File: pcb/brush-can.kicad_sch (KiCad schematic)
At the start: 30 parts, among them J1 Conn_ARM_SWD_TagConnect_TC203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, J2 Conn_01x04_MountingPin, J3 Conn_01x04_MountingPin, U1 AP62150Z6, U2 NCP176, U3 STM32G431CBUx, U4 TJA1044GTK/3, Y1 16MHz

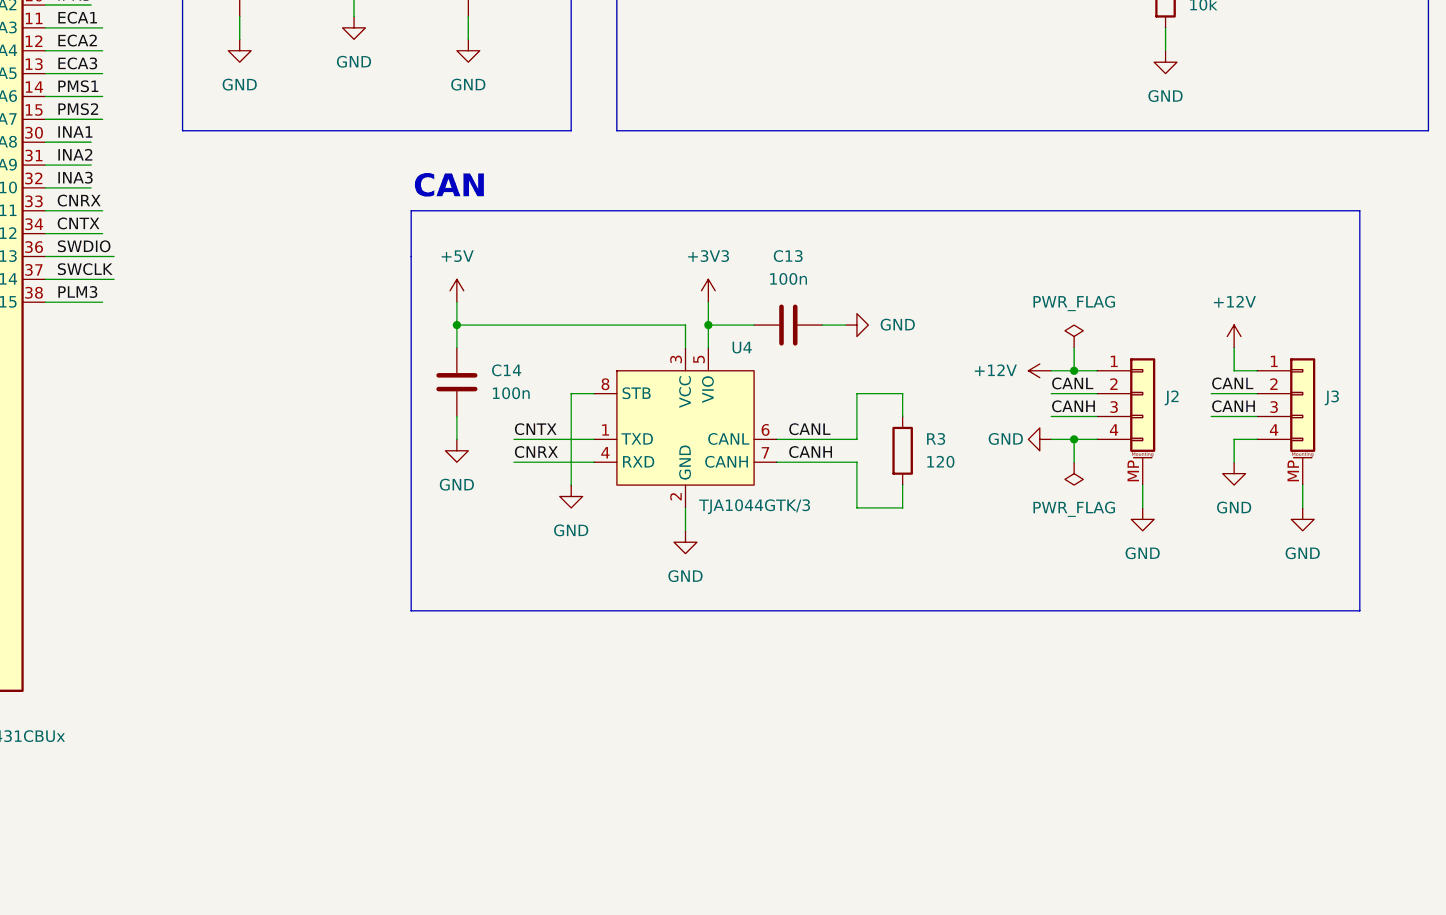
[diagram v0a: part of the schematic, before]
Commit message: Add inserts and change CAN connection
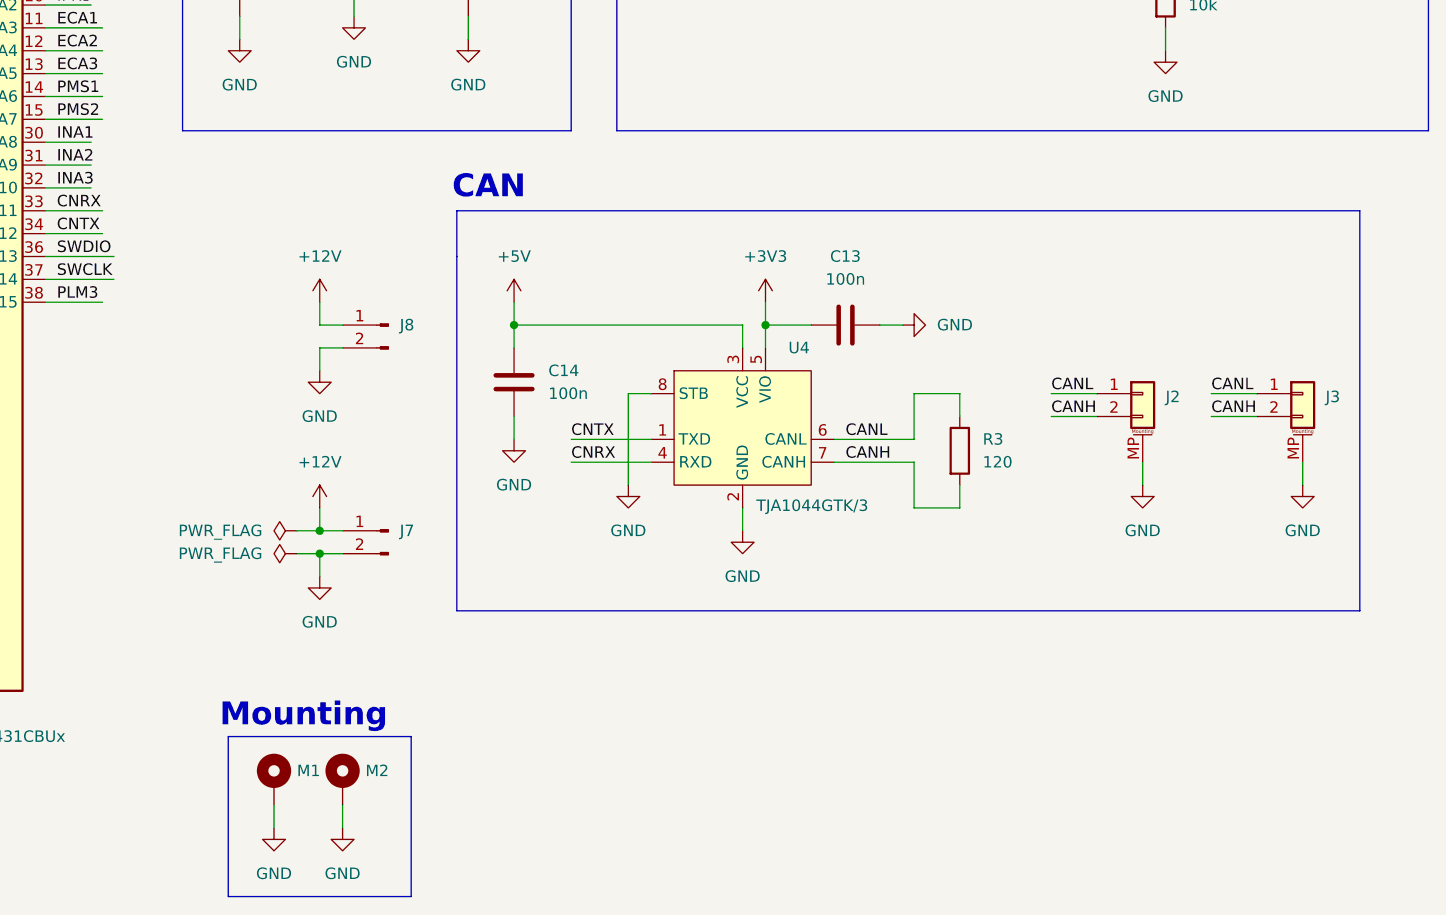
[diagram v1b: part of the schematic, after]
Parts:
- removed J2, J3: Conn_01x04_MountingPin, Connector_JST:JST_GH_SM04B-GHS-TB_1x04-1MP_P1.25mm_Horizontal, symbol Connector_Generic_MountingPin:Conn_01x04_MountingPin
- added J2, J3: Conn_01x02_MountingPin, Connector_JST:JST_SH_SM02B-SRSS-TB_1x02-1MP_P1.00mm_Horizontal, symbol Connector_Generic_MountingPin:Conn_01x02_MountingPin
- added J7, J8: Conn_01x02_Pin, Connector_PinHeader_2.54mm:PinHeader_1x02_P2.54mm_Vertical, symbol Connector:Conn_01x02_Pin
- added M1, M2: 24939, User_Footprints:24939, symbol User_Symbols:24939
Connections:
- net +12V: now also J7.1 (Pin_1), J8.1 (Pin_1)
- net CANH: now also J2.2 (Pin_2), J3.2 (Pin_2)
- net CANL: now also J2.1 (Pin_1), J3.1 (Pin_1)
- net GND: now also J2.MP (MountPin), J3.MP (MountPin), J7.2 (Pin_2), J8.2 (Pin_2), M1.MP, M2.MP
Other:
- note added: "Mounting"
- moved on the sheet: C13, C14, R3, U4

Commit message: Finish layout
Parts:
- removed C2: 100n, Capacitor_SMD:C_0402_1005Metric, symbol Device:C
- C1: footprint Capacitor_SMD:C_0603_1608Metric -> Capacitor_SMD:C_0402_1005Metric
- J7, J8: footprint Connector_PinHeader_2.54mm:PinHeader_1x02_P2.54mm_Vertical -> User_Footprints:PowerPins
- L1: footprint Inductor_SMD:L_Sunlord_MWSA0412S -> Inductor_SMD:L_Chilisin_BMRA00040420; LCSC (none) -> C207829
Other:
- moved on the sheet: C1
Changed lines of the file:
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@@
 	)
 	(junction
-		(at 33.02 78.74)
-		(diameter 0)
-		(color 0 0 0 0)
-	)
-	(junction
 		(at 109.22 81.28)
 		(diameter 0)
@@
 	)
 	(junction
-		(at 45.72 66.04)
-		(diameter 0)
-		(color 0 0 0 0)
-	)
-	(junction
 		(at 264.16 71.12)
 		(diameter 0)
@@
 	(wire
 		(pts
-			(xy 33.02 66.04) (xy 45.72 66.04)
-		)
-		(stroke
-			(width 0)
-			(type default)
-		)
-	)
-	(wire
-		(pts
 			(xy 82.55 35.56) (xy 88.9 35.56)
 		)
@@
 	(wire
 		(pts
+			(xy 45.72 78.74) (xy 45.72 81.28)
+		)
+		(stroke
+			(width 0)
+			(type default)
+		)
+	)
+	(wire
+		(pts
 			(xy 90.17 129.54) (xy 96.52 129.54)
 		)
@@
 	(wire
 		(pts
-			(xy 33.02 78.74) (xy 45.72 78.74)
-		)
-		(stroke
-			(width 0)
-			(type default)
-		)
-	)
-	(wire
-		(pts
 			(xy 129.54 121.92) (xy 137.16 121.92)
 		)
@@
 	(wire
 		(pts
-			(xy 33.02 78.74) (xy 33.02 81.28)
-		)
-		(stroke
-			(width 0)
-			(type default)
-		)
-	)
-	(wire
-		(pts
 			(xy 44.45 166.37) (xy 41.91 166.37)
 		)
@@
 	(wire
 		(pts
-			(xy 33.02 68.58) (xy 33.02 66.04)
-		)
-		(stroke
-			(width 0)
-			(type default)
-		)
-	)
-	(wire
-		(pts
 			(xy 129.54 114.3) (xy 134.62 114.3)
 		)
@@
 	(wire
 		(pts
-			(xy 33.02 78.74) (xy 33.02 76.2)
-		)
-		(stroke
-			(width 0)
-			(type default)
-		)
-	)
-	(wire
-		(pts
 			(xy 133.35 27.94) (xy 139.7 27.94)
 		)
@@
 	)
 	(symbol
-		(lib_id "Device:C")
-		(at 45.72 72.39 0)
-		(unit 1)
-		(exclude_from_sim no)
-		(in_bom yes)
-		(on_board yes)
-		(dnp no)
-		(fields_autoplaced yes)
-		(property "Reference" "C2"
-			(at 49.53 71.12 0)
-			(effects
-				(font
-					(size 1.27 1.27)
-				)
-				(justify left)
-			)
-		)
-		(property "Value" "100n"
-			(at 49.53 73.66 0)
-			(effects
-				(font
-					(size 1.27 1.27)
-				)
-				(justify left)
-			)
-		)
-		(property "Footprint" "Capacitor_SMD:C_0402_1005Metric"
-			(at 46.6852 76.2 0)
-			(effects
-				(font
-					(size 1.27 1.27)
-				)
-				(hide yes)
-			)
-		)
-		(property "Datasheet" "~"
-			(at 45.72 72.39 0)
-			(effects
-				(font
-					(size 1.27 1.27)
-				)
-				(hide yes)
-			)
-		)
-		(property "Description" ""
-			(at 45.72 72.39 0)
-			(effects
-				(font
-					(size 1.27 1.27)
-				)
-				(hide yes)
-			)
-		)
-		(pin "1"
-		)
-		(pin "2"
-		)
-		(instances
-			(project "brush-can"
-				(path "/91e4682e-33ab-4e83-b6e9-9501af34d25d"
-					(reference "C2")
-					(unit 1)
-				)
-			)
-		)
-	)
-	(symbol
 		(lib_id "power:GND")
 		(at 181.61 142.24 0)
@@
 			)
 		)
-		(property "Footprint" "Inductor_SMD:L_Sunlord_MWSA0412S"
+		(property "Footprint" "Inductor_SMD:L_Chilisin_BMRA00040420"
 			(at 247.65 71.12 0)
 			(effects
@@
 			)
 		)
+		(property "LCSC" "C207829"
+			(at 247.65 71.12 90)
+			(effects
+				(font
+					(size 1.27 1.27)
+				)
+				(hide yes)
+			)
+		)
 		(pin "1"
 		)
@@
 	(symbol
 		(lib_id "Device:C")
-		(at 33.02 72.39 0)
+		(at 45.72 72.39 0)
 		(unit 1)
 		(exclude_from_sim no)
@@
 		(fields_autoplaced yes)
 		(property "Reference" "C1"
-			(at 36.83 71.12 0)
+			(at 49.53 71.12 0)
 			(effects
 				(font
@@
 		)
 		(property "Value" "10u"
-			(at 36.83 73.66 0)
+			(at 49.53 73.66 0)
 			(effects
 				(font
@@
 			)
 		)
-		(property "Footprint" "Capacitor_SMD:C_0603_1608Metric"
-			(at 33.9852 76.2 0)
+		(property "Footprint" "Capacitor_SMD:C_0402_1005Metric"
+			(at 46.6852 76.2 0)
 			(effects
 				(font
@@
 		)
 		(property "Datasheet" "~"
-			(at 33.02 72.39 0)
+			(at 45.72 72.39 0)
 			(effects
 				(font
@@
 		)
 		(property "Description" ""
-			(at 33.02 72.39 0)
+			(at 45.72 72.39 0)
 			(effects
 				(font
@@
 	)
 	(symbol
+		(lib_id "power:GND")
+		(at 45.72 81.28 0)
+		(unit 1)
+		(exclude_from_sim no)
+		(in_bom yes)
+		(on_board yes)
+		(dnp no)
+		(fields_autoplaced yes)
+		(property "Reference" "#PWR04"
+			(at 45.72 87.63 0)
+			(effects
+				(font
+					(size 1.27 1.27)
+				)
+				(hide yes)
+			)
+		)
+		(property "Value" "GND"
+			(at 45.72 86.36 0)
+			(effects
+				(font
+					(size 1.27 1.27)
+				)
+			)
+		)
+		(property "Footprint" ""
+			(at 45.72 81.28 0)
+			(effects
+				(font
+					(size 1.27 1.27)
+				)
+				(hide yes)
+			)
+		)
+		(property "Datasheet" ""
+			(at 45.72 81.28 0)
+			(effects
+				(font
+					(size 1.27 1.27)
+				)
+				(hide yes)
+			)
+		)
+		(property "Description" ""
+			(at 45.72 81.28 0)
+			(effects
+				(font
+					(size 1.27 1.27)
+				)
+				(hide yes)
+			)
+		)
+		(pin "1"
+		)
+		(instances
+			(project "brush-can"
+				(path "/91e4682e-33ab-4e83-b6e9-9501af34d25d"
+					(reference "#PWR04")
+					(unit 1)
+				)
+			)
+		)
+	)
+	(symbol
 		(lib_id "Device:C")
 		(at 176.53 91.44 0)
@@
 			)
 		)
-		(property "Footprint" "Connector_PinHeader_2.54mm:PinHeader_1x02_P2.54mm_Vertical"
+		(property "Footprint" "User_Footprints:PowerPins"
 			(at 167.64 129.54 0)
 			(effects
@@
 			)
 		)
-		(property "Footprint" "Connector_PinHeader_2.54mm:PinHeader_1x02_P2.54mm_Vertical"
+		(property "Footprint" "User_Footprints:PowerPins"
 			(at 167.64 152.4 0)
 			(effects
@@
 					(unit 1)
 				)
-			)
-		)
-	)
-	(symbol
-		(lib_id "power:GND")
-		(at 33.02 81.28 0)
-		(unit 1)
-		(exclude_from_sim no)
-		(in_bom yes)
-		(on_board yes)
-		(dnp no)
-		(fields_autoplaced yes)
-		(property "Reference" "#PWR04"
-			(at 33.02 87.63 0)
-			(effects
-				(font
-					(size 1.27 1.27)
-				)
-				(hide yes)
-			)
-		)
-		(property "Value" "GND"
-			(at 33.02 86.36 0)
-			(effects
-				(font
-					(size 1.27 1.27)
-				)
-			)
-		)
-		(property "Footprint" ""
-			(at 33.02 81.28 0)
-			(effects
-				(font
-					(size 1.27 1.27)
-				)
-				(hide yes)
-			)
-		)
-		(property "Datasheet" ""
-			(at 33.02 81.28 0)
-			(effects
-				(font
-					(size 1.27 1.27)
-				)
-				(hide yes)
-			)
-		)
-		(property "Description" ""
-			(at 33.02 81.28 0)
-			(effects
-				(font
-					(size 1.27 1.27)
-				)
-				(hide yes)
-			)
-		)
-		(pin "1"
-		)
-		(instances
-			(project "brush-can"
-				(path "/91e4682e-33ab-4e83-b6e9-9501af34d25d"
-					(reference "#PWR04")
-					(unit 1)
-				)

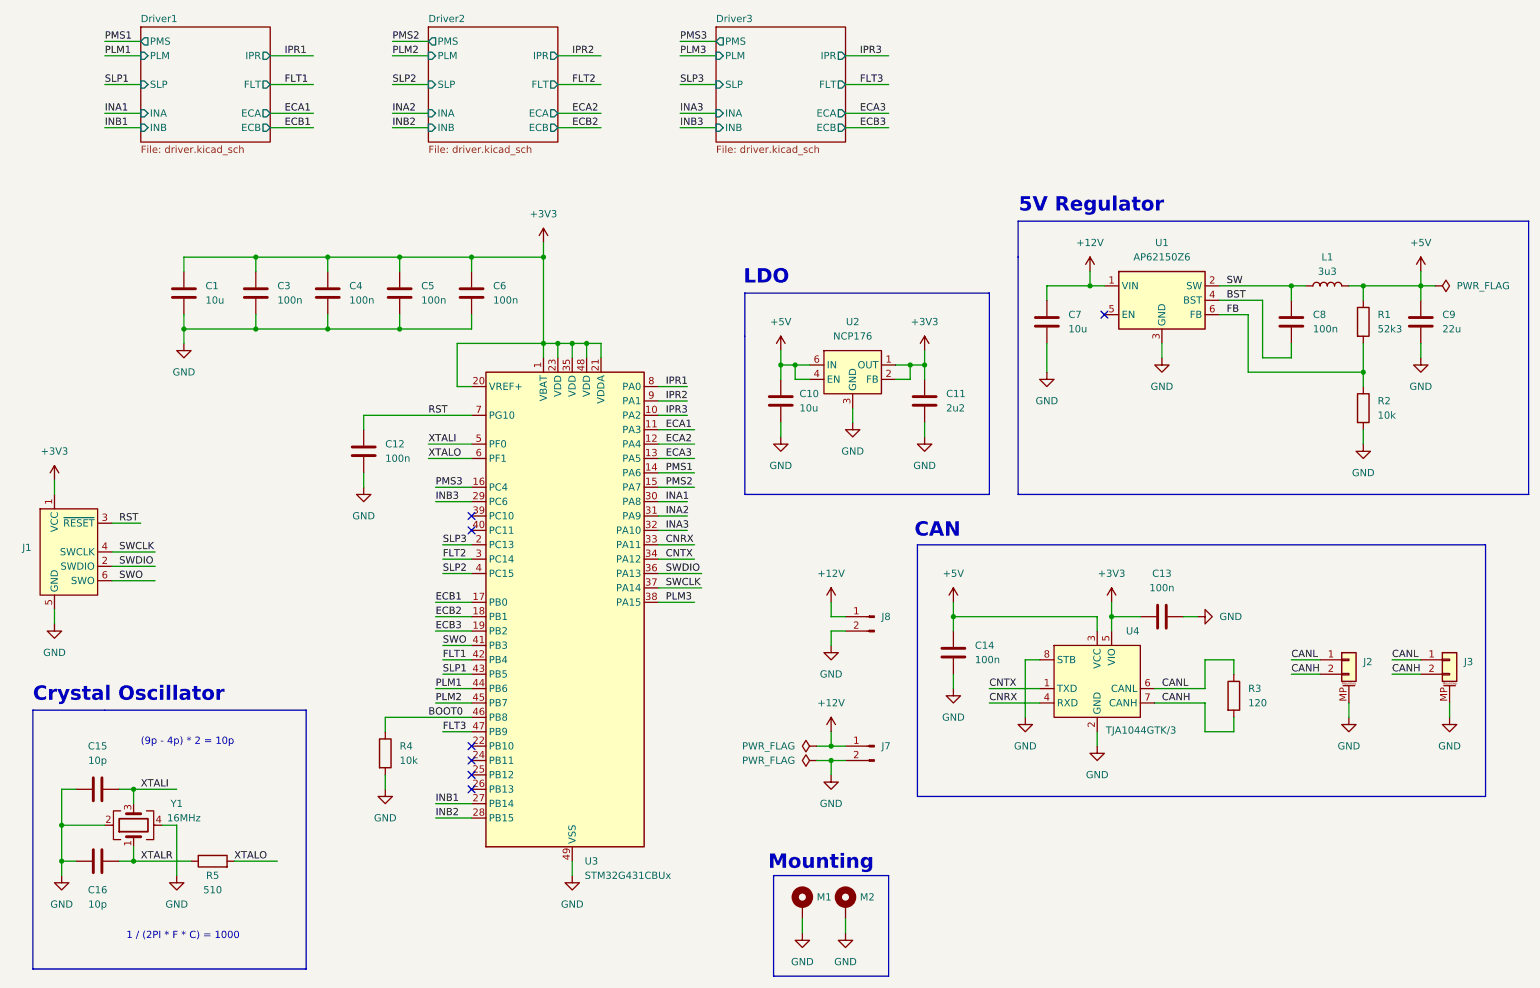
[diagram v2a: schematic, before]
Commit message: Finish routing and rule checking
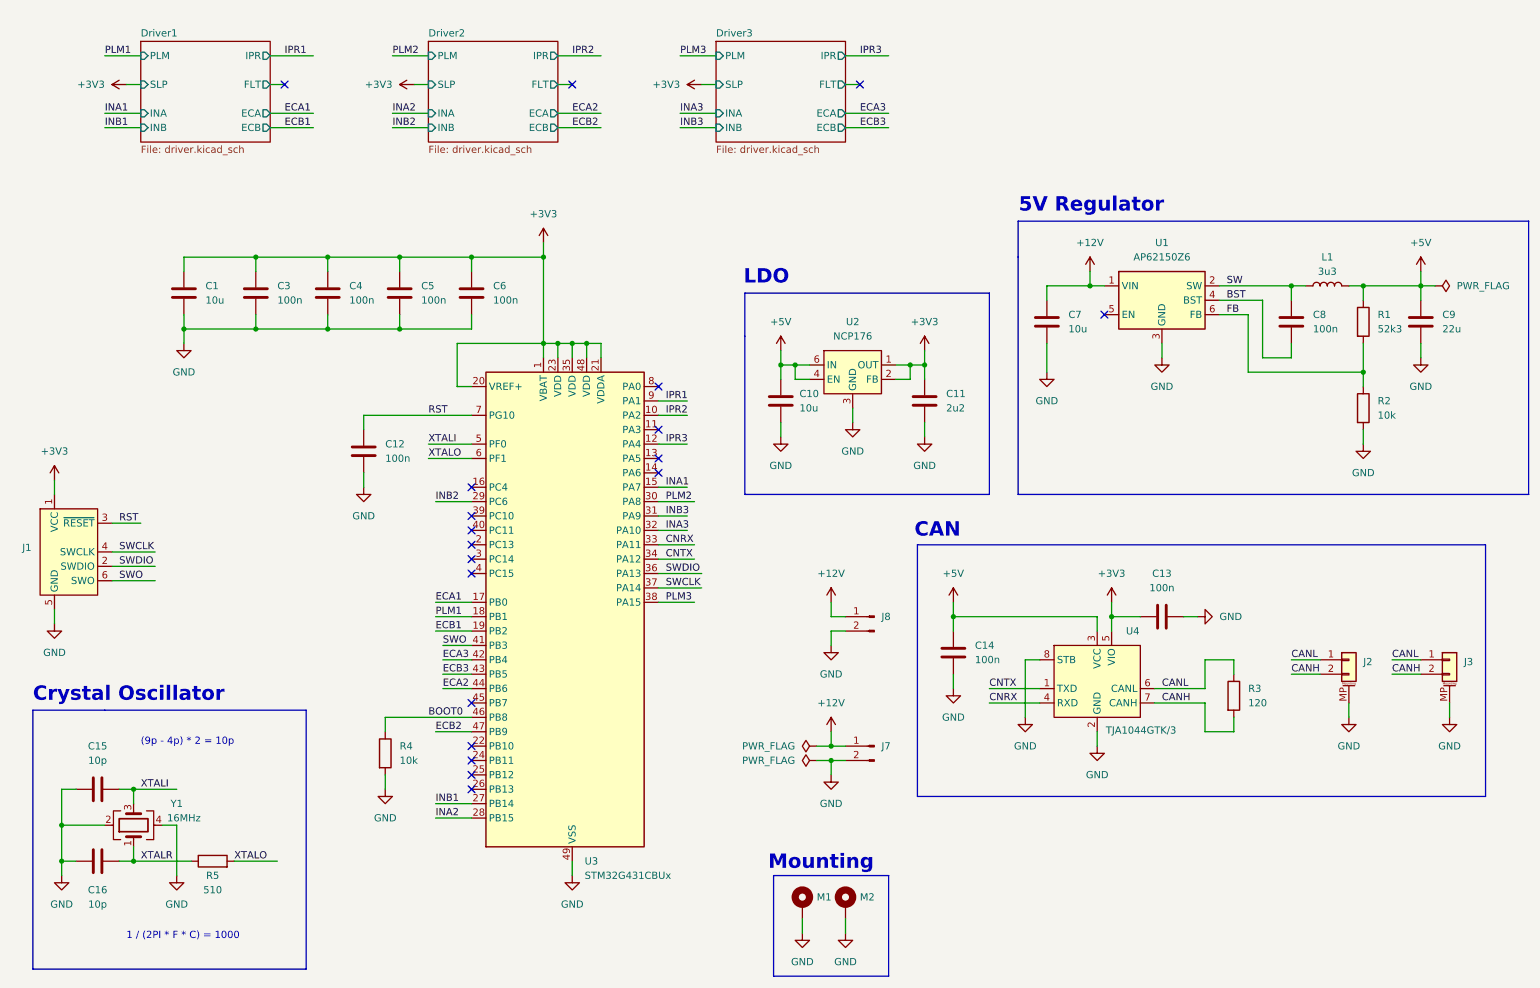
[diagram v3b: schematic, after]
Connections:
- net FLT1 is gone; now on net ECA3: U3.42 (PB4)
- net FLT3 is gone; now on net ECB2: U3.47 (PB9)
- net PMS2 is gone; now on net INA1: U3.15 (PA7)
- net SLP1 is gone; now on net ECB3: U3.43 (PB5)
- net ECA1: now also U3.17 (PB0); no longer U3.11 (PA3)
- net ECA2: now also U3.44 (PB6); no longer U3.12 (PA4)
- net ECA3: no longer U3.13 (PA5)
- net ECB1: now also U3.19 (PB2); no longer U3.17 (PB0)
- net ECB2: no longer U3.18 (PB1)
- net ECB3: no longer U3.19 (PB2)
- net INA1: no longer U3.30 (PA8)
- net INA2: now also U3.28 (PB15); no longer U3.31 (PA9)
- net INB2: now also U3.29 (PC6); no longer U3.28 (PB15)
- net INB3: now also U3.31 (PA9); no longer U3.29 (PC6)
- net IPR1: now also U3.9 (PA1); no longer U3.8 (PA0)
- net IPR2: now also U3.10 (PA2); no longer U3.9 (PA1)
- net IPR3: now also U3.12 (PA4); no longer U3.10 (PA2)
- net PLM1: now also U3.18 (PB1); no longer U3.44 (PB6)
- net PLM2: now also U3.30 (PA8); no longer U3.45 (PB7)
- net FLT2: no longer names the net of U3.3 (PC14)
- net PMS1: no longer names the net of U3.14 (PA6)
- net PMS3: no longer names the net of U3.16 (PC4)
- net SLP2: no longer names the net of U3.4 (PC15)
- net SLP3: no longer names the net of U3.2 (PC13)
- no-connect marks 7 -> 19
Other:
- sheet Driver1 ports: added none; removed PMS
- sheet Driver2 ports: added none; removed PMS
- sheet Driver3 ports: added none; removed PMS

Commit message: Finish final details
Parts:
- J2, J3: LCSC (none) -> C160402
- J7, J8, M1, M2: now not fitted
- R1: value 52k3 -> 56k
- U3: LCSC (none) -> C529356
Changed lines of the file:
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@@
 			)
 		)
+		(property "LCSC" "C160402"
+			(at 269.24 137.16 0)
+			(effects
+				(font
+					(size 1.27 1.27)
+				)
+				(hide yes)
+			)
+		)
 		(pin "1"
 		)
@@
 		(in_bom yes)
 		(on_board yes)
-		(dnp no)
+		(dnp yes)
 		(fields_autoplaced yes)
 		(property "Reference" "M2"
@@
 			)
 		)
-		(property "Value" "52k3"
+		(property "Value" "56k"
 			(at 256.54 78.7399 0)
 			(effects
@@
 			)
 		)
+		(property "LCSC" "C160402"
+			(at 251.46 137.16 0)
+			(effects
+				(font
+					(size 1.27 1.27)
+				)
+				(hide yes)
+			)
+		)
 		(pin "1"
 		)
@@
 			)
 		)
+		(property "LCSC" "C529356"
+			(at 111.76 129.54 0)
+			(effects
+				(font
+					(size 1.27 1.27)
+				)
+				(hide yes)
+			)
+		)
 		(pin "21"
 		)
@@
 		(in_bom yes)
 		(on_board yes)
-		(dnp no)
+		(dnp yes)
 		(fields_autoplaced yes)
 		(property "Reference" "J8"
@@
 		(in_bom yes)
 		(on_board yes)
-		(dnp no)
+		(dnp yes)
 		(fields_autoplaced yes)
 		(property "Reference" "J7"
@@
 		(in_bom yes)
 		(on_board yes)
-		(dnp no)
+		(dnp yes)
 		(fields_autoplaced yes)
 		(property "Reference" "M1"

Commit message: Edit lcsc part number
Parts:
- C7: LCSC C19702 -> C96446
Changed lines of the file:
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@@
 			)
 		)
-		(property "LCSC" "C19702"
+		(property "LCSC" "C96446"
 			(at 198.12 77.47 0)
 			(effects

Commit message: Save
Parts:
- U2: LCSC (none) -> C233363
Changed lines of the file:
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@@
+			)
+		)
+		(property "LCSC" "C233363"
+			(at 163.83 85.09 0)
+			(effects
+				(font
+					(size 1.27 1.27)
+				)
+				(hide yes)
 			)
 		)
